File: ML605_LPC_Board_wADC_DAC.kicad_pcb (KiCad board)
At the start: 4 copper layers, 100.1 x 99.7 mm, 122 parts, among them IC1 ADC10D040CIVS_NOPB, IC2 AD8137YRZ-REEL, IC3 AD8137YRZ-REEL, IC4 DAC5652IPFB, J1 ASP-134604-01, J10 Conn_02x06_Odd_Even, J11 Conn_02x06_Odd_Even, J12 Conn_02x06_Odd_Even, J13 Conn_01x03_Pin, J14 Conn_01x03_Pin, J2 Conn_01x03_Pin, J3 Conn_01x03_Pin, J4 SMA Connector, J5 SMA Connector, J6 Conn_01x03_Pin, J7 Conn_01x03_Pin, J8 SMA Connector, J9 SMA Connector, U1 LMV7219M7, U2 LMV7219M7, U3 NCV317, U4 LMH6720MA, U5 LMH6720MA

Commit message: Fixed pcb dimensions (again)
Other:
- board size 100.1 x 99.7 mm -> 99.9 x 99.7 mm
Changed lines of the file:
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@@
 		(pts
 			(xy 90.875 139.205) (xy 75 139.205) (xy 75 59.83) (xy 90.875 59.83) (xy 92.78 57.925) (xy 92.78 49.67)
-			(xy 175.076 49.67) (xy 175.076 149.365) (xy 92.78 149.365) (xy 92.78 141.11)
+			(xy 174.949 49.67) (xy 174.949 149.365) (xy 92.78 149.365) (xy 92.78 141.11)
 		)
 		(stroke
@@
 		(polygon
 			(pts
-				(xy 75 49.67) (xy 175.076 49.67) (xy 175.076 149.365) (xy 75 149.365)
+				(xy 75 49.67) (xy 174.949 49.67) (xy 174.949 149.365) (xy 75 149.365)
 			)
 		)

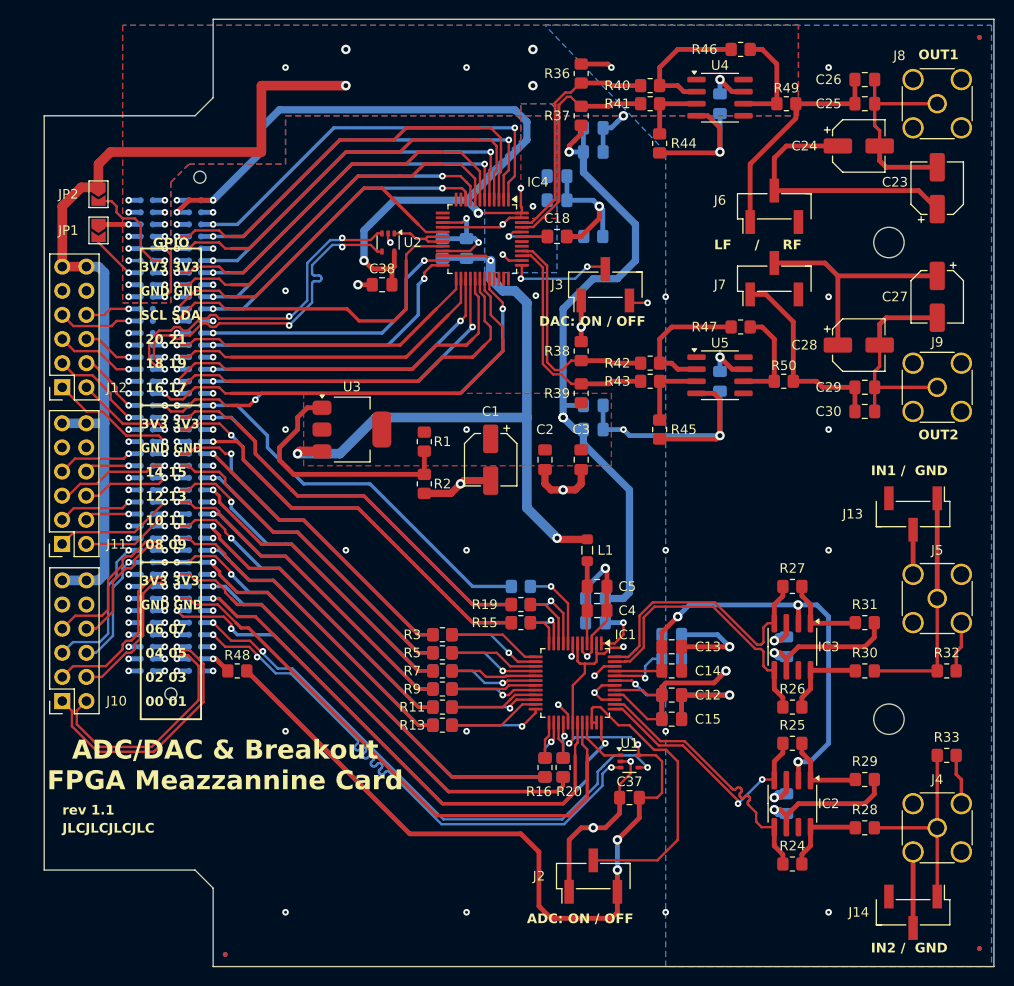
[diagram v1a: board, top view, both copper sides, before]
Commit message: Added identification EEPROM to comply with the 2019 revision of the VITA 57.1 standard
The EEPROM and its complementary components are marked as DNP, as they are not necessary for the ML602 board to function
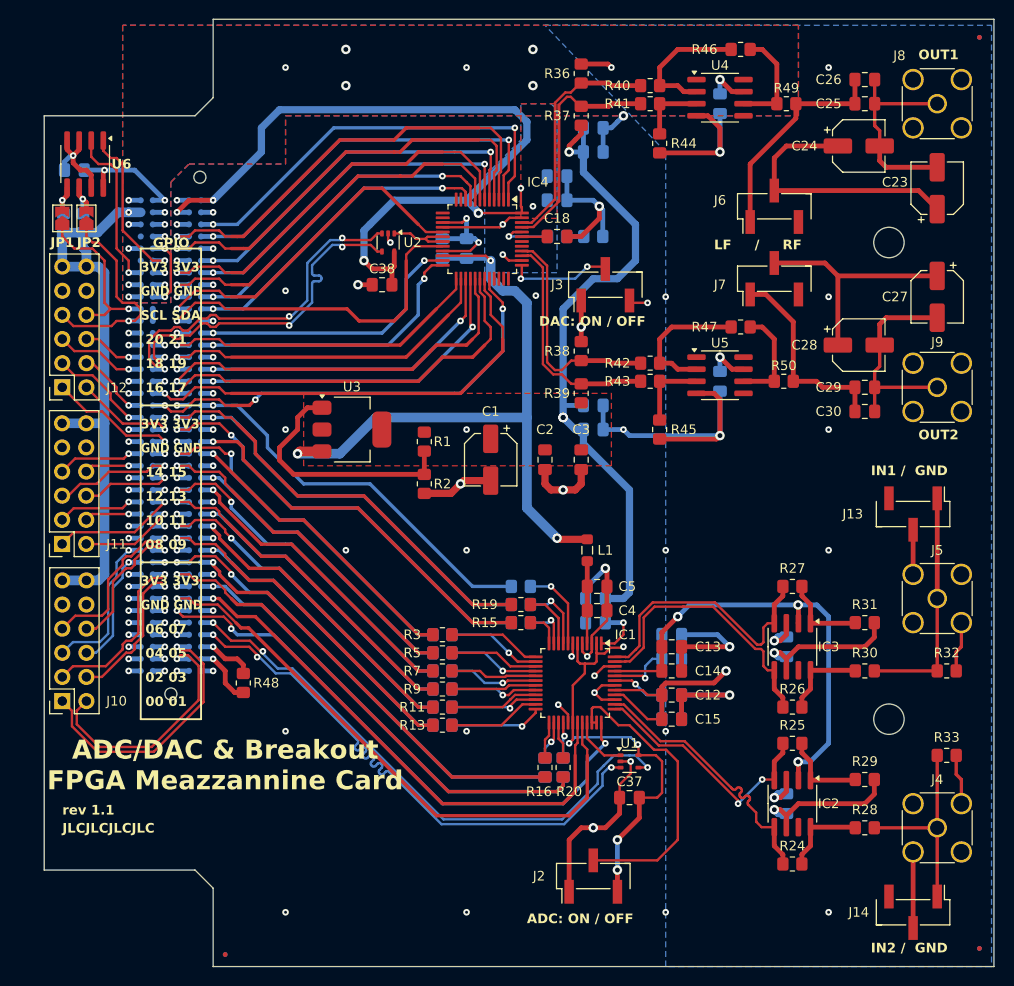
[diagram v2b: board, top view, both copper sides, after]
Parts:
- added C39: 100n, Capacitor_SMD:C_0805_2012Metric_Pad1.18x1.45mm_HandSolder, B.Cu at (78.2, 65.5)
- added R51: 5k, Resistor_SMD:R_0805_2012Metric_Pad1.20x1.40mm_HandSolder, B.Cu at (77.0, 71.1)
- added R52: 5k, Resistor_SMD:R_0805_2012Metric_Pad1.20x1.40mm_HandSolder, B.Cu at (79.1, 71.1)
- added U6: M24C02-FMN, Package_SO:SOIC-8_3.9x4.9mm_P1.27mm, F.Cu at (79.3, 64.9)
- moved JP1 4.02 mm to (76.9, 70.6), turned to 90 degrees
- moved JP2 2.84 mm to (79.4, 70.6), turned to 90 degrees
- moved R48 1.42 mm to (96.0, 119.5), turned to 90 degrees
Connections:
- net /LA01_N_CC renamed /LA01_N
- net /LA01_P_CC renamed /LA01_P
- J1 pad D31: /TDO -> /TDI
- JP1 pad 1: GNDA -> /SDA
- JP1 pad 2: /GA0 -> /Identification_EEPROM/SDA
- JP2 pad 1: 3V3 -> /SCL
- JP2 pad 2: /GA1 -> /Identification_EEPROM/SCL
- R48 pad 2: VADJ -> GNDA
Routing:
- net VADJ: track 253.0 -> 197.4 mm
- net 3V3: track 226.9 -> 206.7 mm, vias 19 -> 20
- net /SCL: track 8.97 -> 23.4 mm
- net /SDA: track 5.98 -> 18.0 mm
- net GNDA: track 325.0 -> 336.9 mm, vias 108 -> 109
- net /GA0: track 6.31 -> 17.6 mm
- net /GA1: track 12.5 -> 17.5 mm
- net /Identification_EEPROM/SCL: track 0.00 -> 4.37 mm, vias 0 -> 1
- net /Identification_EEPROM/SDA: track 0.00 -> 4.19 mm, vias 0 -> 1
- net /PRSNT_M2C_L: track 3.34 -> 6.66 mm
- net +12V: track 2.54 -> 0.00 mm, vias 2 -> 0
- net /TDI: track 0.00 -> 1.27 mm

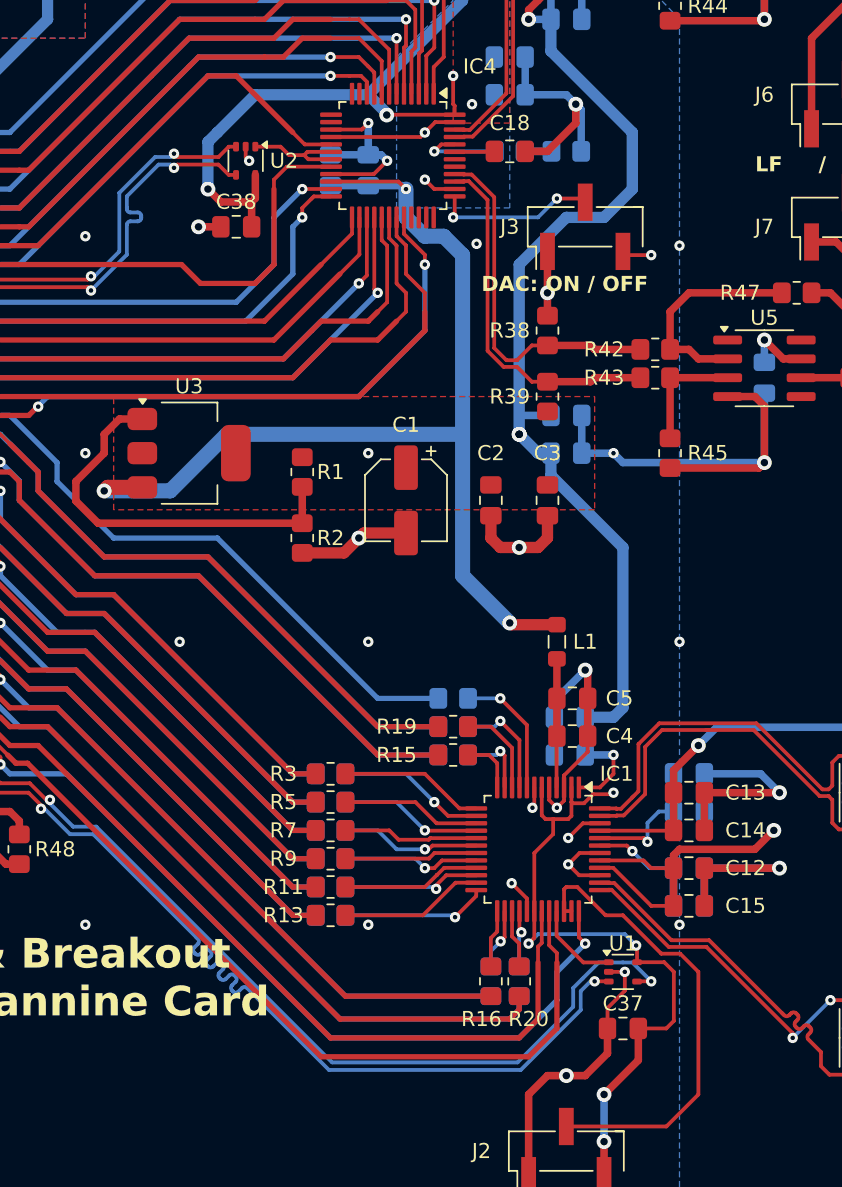
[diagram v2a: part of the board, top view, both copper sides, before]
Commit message: Changed clock comparators to dedicated LVDS decoders and changed ADC Vdd inductor to ferrite bead
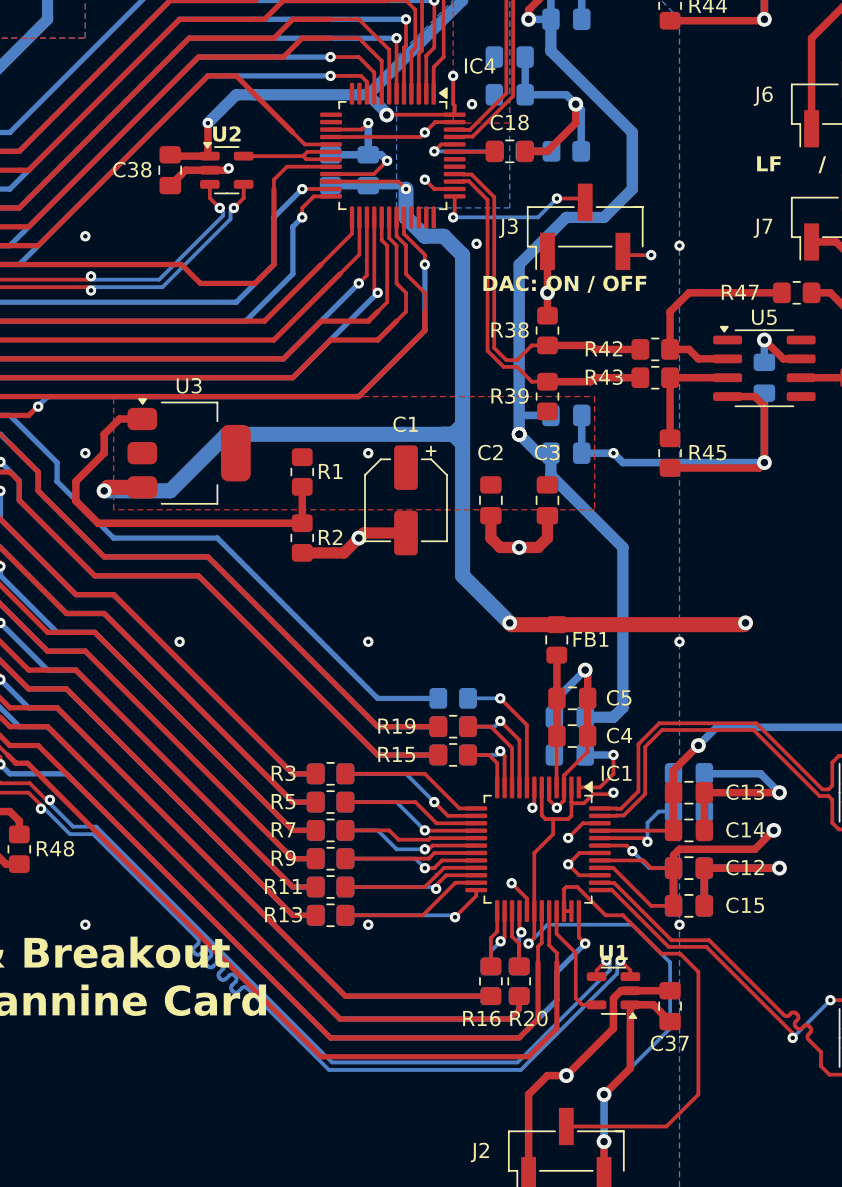
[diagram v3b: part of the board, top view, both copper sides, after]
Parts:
- removed L1: 100u, Inductor_SMD:L_0805_2012Metric_Pad1.05x1.20mm_HandSolder
- added FB1: 180@100MHz, Inductor_SMD:L_0805_2012Metric_Pad1.15x1.40mm_HandSolder, F.Cu at (132.1, 105.4)
- U1, U2: value LMV7219M7 -> SN65LVDS2DBV; footprint Package_TO_SOT_SMD:SOT-353_SC-70-5 -> Package_TO_SOT_SMD:SOT-23-5
- moved C38 5.85 mm to (106.1, 73.8), turned to 90 degrees
- moved C37 3.51 mm to (139.8, 130.1), turned to -90 degrees
- moved U2 1.42 mm to (109.9, 73.8), turned to 0 degrees
- moved U1 1.42 mm to (136.0, 129.0), turned to 180 degrees
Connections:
- U1 pad 1: /ADC_Circuit/CLK -> VADJ
- U1 pad 5: VADJ -> /ADC_Circuit/CLK
- U2 pad 1: /DAC Circuit/CLKA/CLKIQ -> VADJ
- U2 pad 5: VADJ -> /DAC Circuit/CLKA/CLKIQ
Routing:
- net 3V3: track 206.7 -> 221.9 mm, vias 20 -> 21
- net /LA26_N: track 37.4 -> 33.9 mm
- net /CLK0_M2C_N: track 60.7 -> 57.6 mm
- net VADJ: track 197.4 -> 200.5 mm, vias 11 -> 10
- net /LA26_P: track 37.4 -> 34.8 mm
- net /CLK0_M2C_P: track 60.6 -> 62.9 mm
- net /ADC_Circuit/CLK: track 5.93 -> 7.99 mm
- net GNDA: track 336.9 -> 338.9 mm, vias 109 -> 107
- net /DAC Circuit/CLKA/CLKIQ: track 7.35 -> 7.96 mm

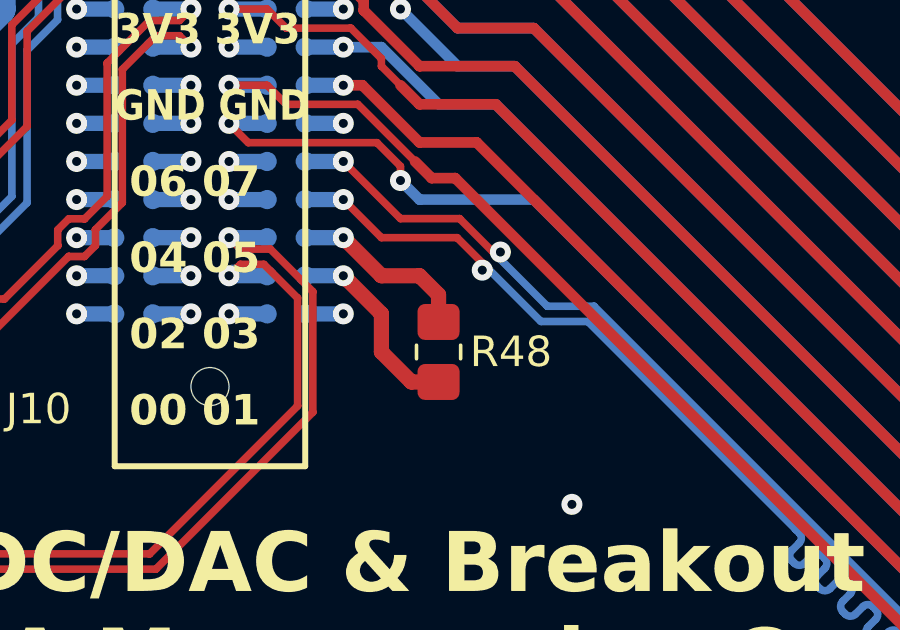
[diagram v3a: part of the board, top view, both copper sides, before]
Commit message: Tied PRSNT pin directly to ground without resistor, fixed reference of J1
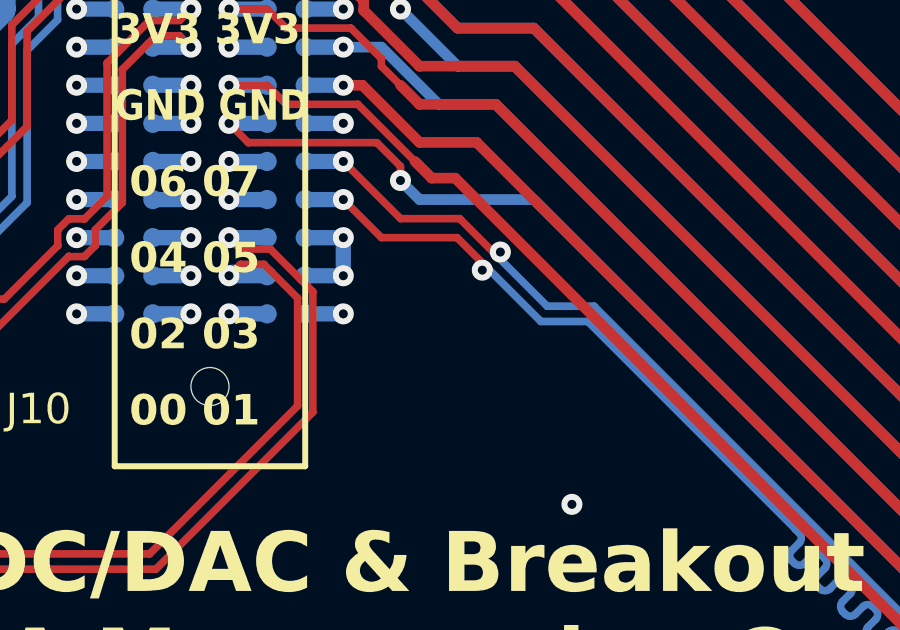
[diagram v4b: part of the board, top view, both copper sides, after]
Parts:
- removed R48: 1k, Resistor_SMD:R_0805_2012Metric_Pad1.20x1.40mm_HandSolder
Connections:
- J1 pad H2: /PRSNT_M2C_L -> GNDA
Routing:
- net /PRSNT_M2C_L: track 6.66 -> 0.00 mm, vias 1 -> 0
- net GNDA: track 338.9 -> 336.6 mm, vias 107 -> 108

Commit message: Rev 1.1 final version
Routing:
- net /CLK0_M2C_P: track 62.9 -> 58.1 mm
- net /LA26_N: track 33.9 -> 34.7 mm
